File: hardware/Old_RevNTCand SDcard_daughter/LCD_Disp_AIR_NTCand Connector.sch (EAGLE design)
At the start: 10 parts

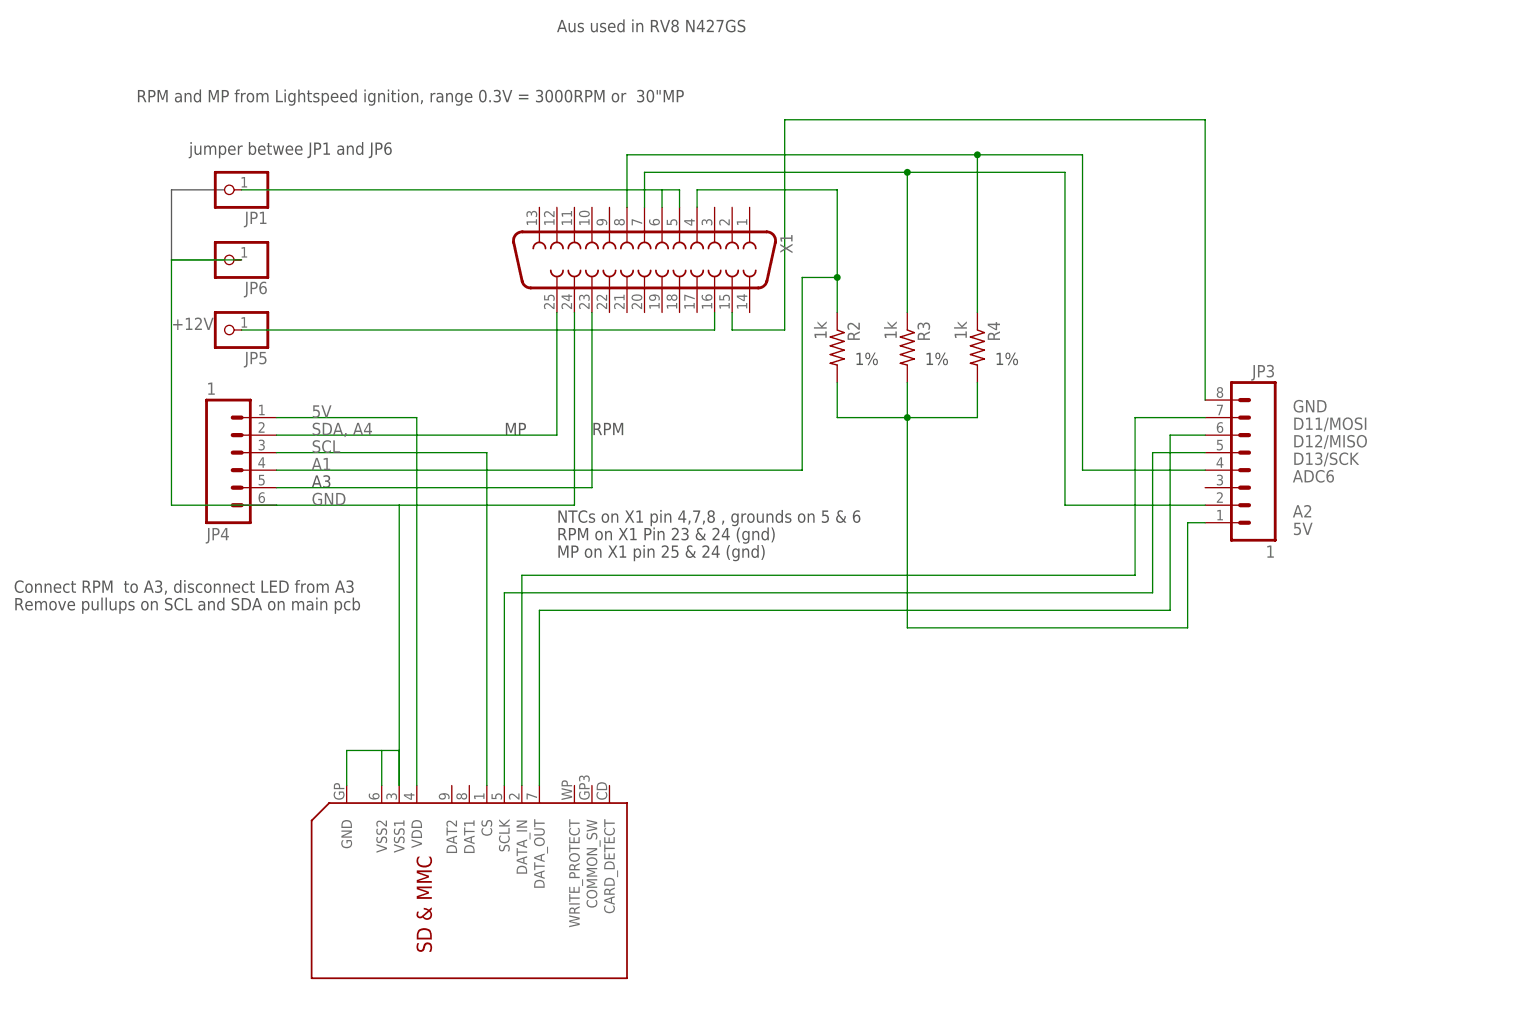
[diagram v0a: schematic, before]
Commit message: Added Fuel pressure reading and external alarm output to 3x Oil NTC temp instrument fixed schematics for incorrect pinout on X1 connector
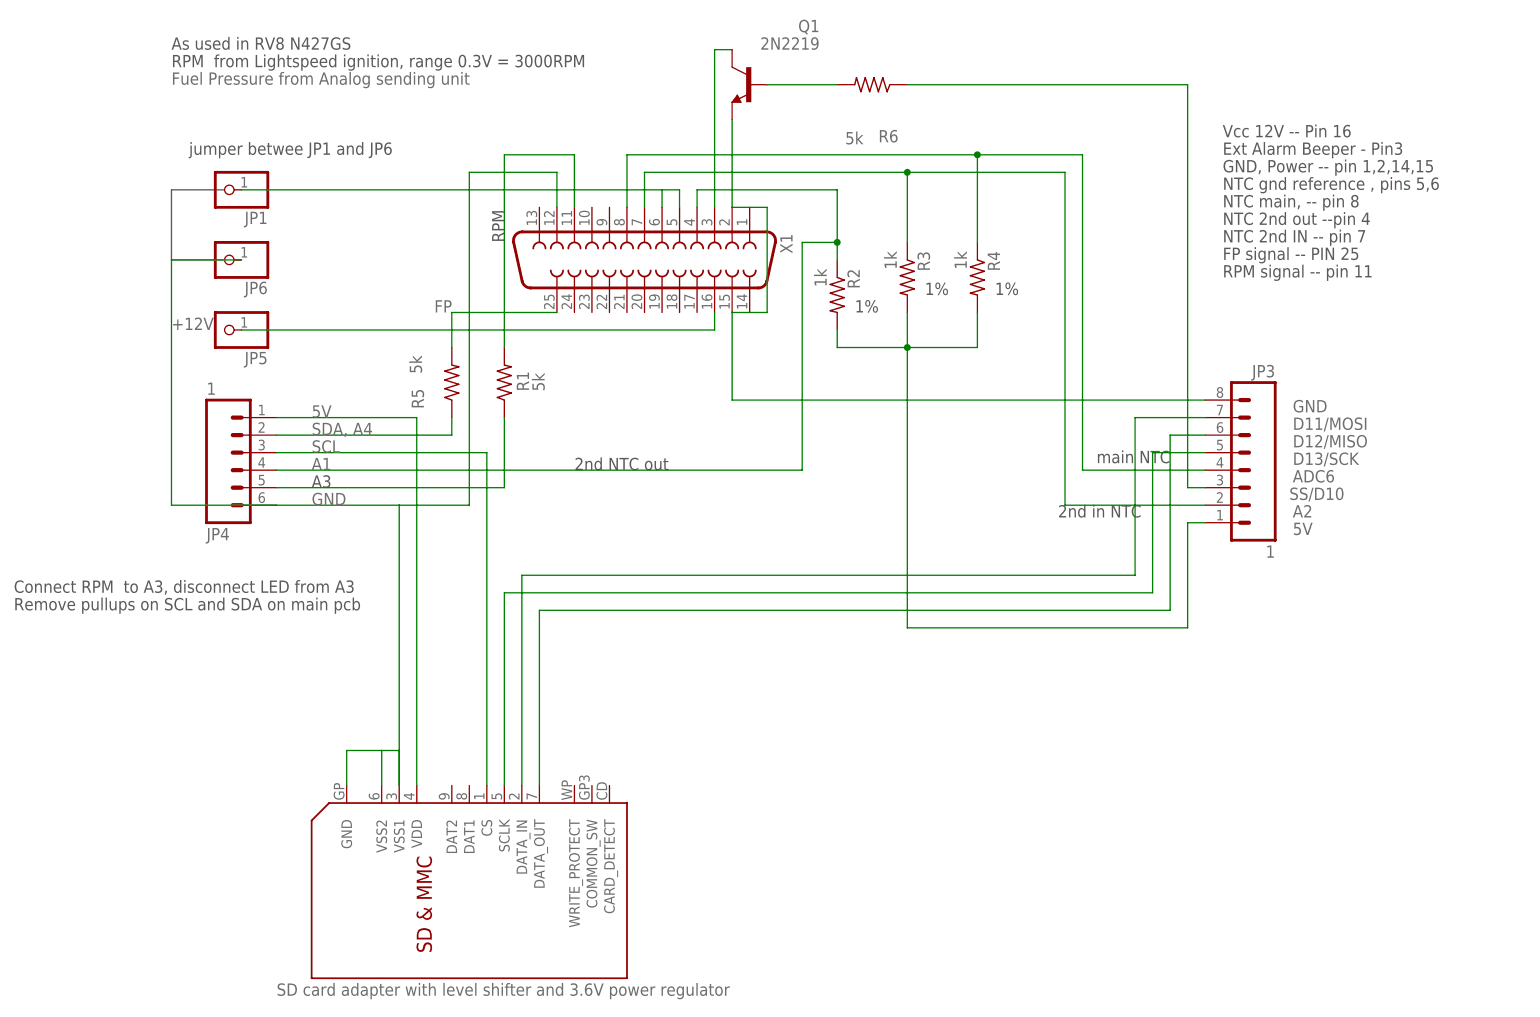
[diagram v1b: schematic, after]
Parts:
- added Q1: 2N2219, transistor-npn:2N2219
- added R1, R5, R6: 5k, rcl:R-US_M0805
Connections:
- new net N$1: R5.2, X1.25
- new net N$13: Q1.C
- new net N$14: Q1.B, R6.2
- new net N$15: JP3.3, R6.1
- new net N$7: R1.2, X1.11
- net GND: now also X1.12; no longer X1.24
- net N$4: now also Q1.E, X1.1, X1.14, X1.2
- net N$5: now also R1.1; no longer X1.23
- net N$6: now also R5.1; no longer X1.25
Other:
- note added: "2nd NTC out"
- note added: "2nd in NTC"
- note added: "As used in RV8 N427GS"
- note added: "Ext Alarm Beeper - Pin3"
- note added: "FP"
- note added: "FP signal -- PIN 25"
- note added: "Fuel Pressure from Analog sending unit"
- note added: "GND, Power -- pin 1,2,14,15"
- note added: "NTC 2nd IN -- pin 7"
- note added: "NTC 2nd out --pin 4"
- note added: "NTC gnd reference , pins 5,6"
- note added: "NTC main, -- pin 8"
- note added: "RPM from Lightspeed ignition, range 0.3V = 3000RPM"
- note added: "RPM signal -- pin 11"
- note added: "SD card adapter with level shifter and 3.6V power regulator"
- note added: "SS/D10"
- note added: "Vcc 12V -- Pin 16"
- note added: "main NTC"
- note removed: "Aus used in RV8 N427GS"
- note removed: "MP"
- note removed: "MP on X1 pin 25 & 24 (gnd)"
- note removed: "NTCs on X1 pin 4,7,8 , grounds on 5 & 6"
- note removed: "RPM and MP from Lightspeed ignition, range 0.3V = 3000RPM or 30"MP"
- note removed: "RPM on X1 Pin 23 & 24 (gnd)"
- moved on the sheet: R2, R3, R4
